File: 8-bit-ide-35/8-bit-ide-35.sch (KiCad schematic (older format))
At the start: 33 parts, among them J1 XTA_Connector, J2 IBM_8bit_DBA, J3 XTA Power, J4 LED, J5 Debug, SW1 Config, SW2 Init Drive, SW3 Reset, U1 74LVC245, U2 74LVC245, U3 74HCT125, U4 RPI_PICO, U5 74HC165

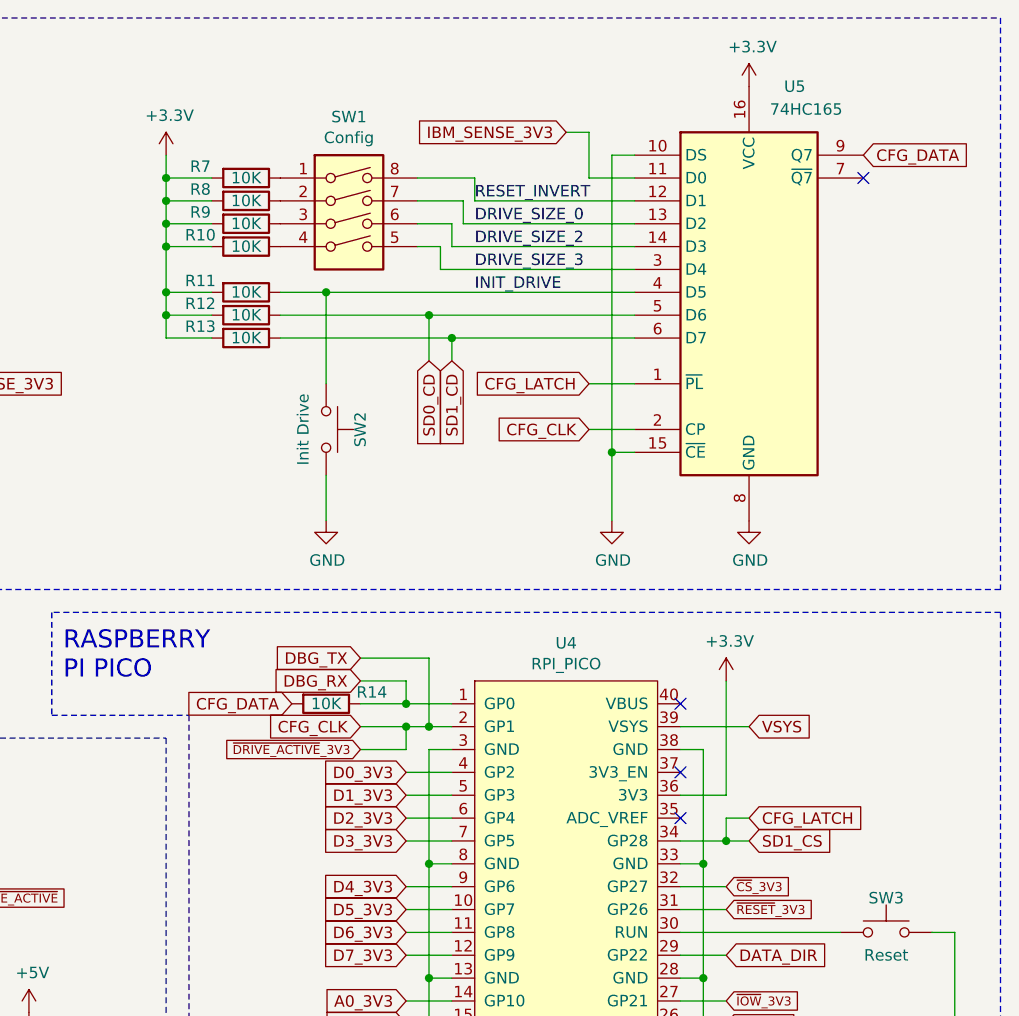
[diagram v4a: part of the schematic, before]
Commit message: Small schematic changes. Add outline of XTA board.
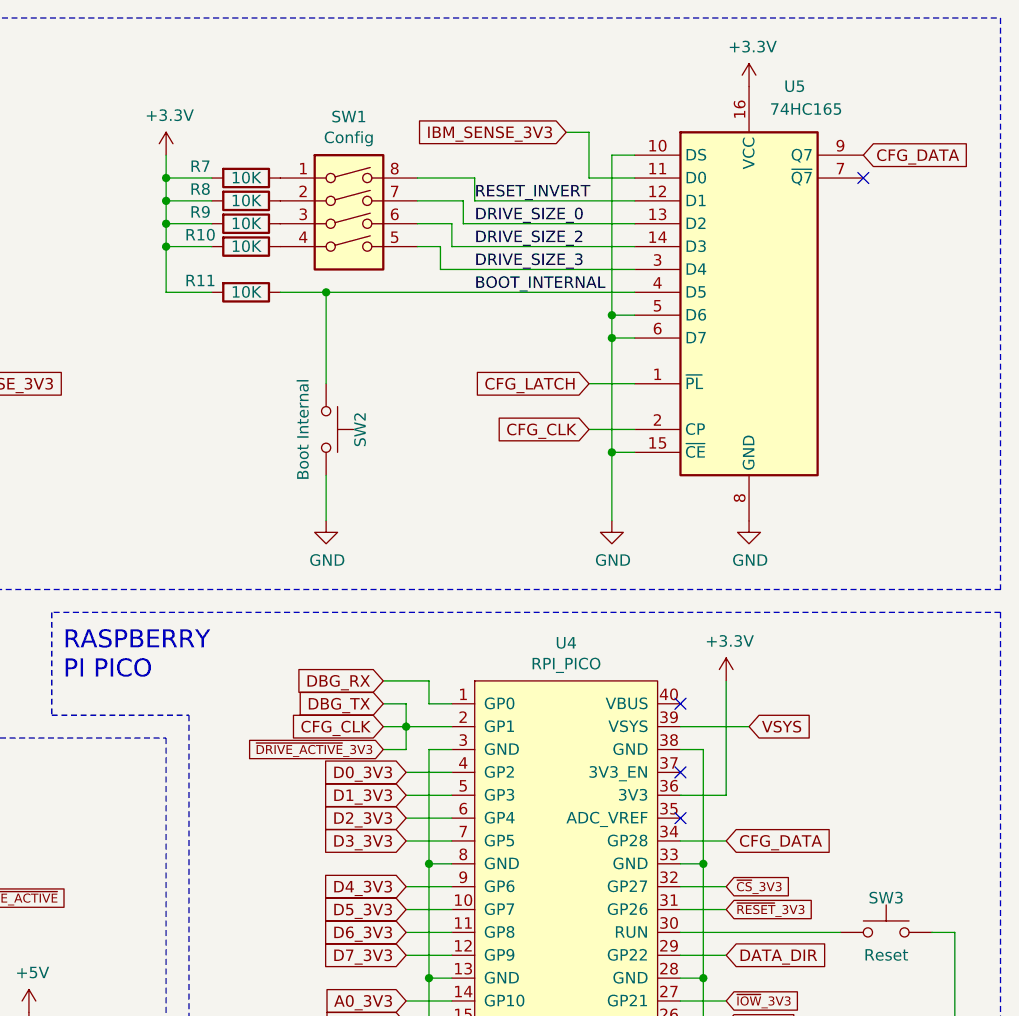
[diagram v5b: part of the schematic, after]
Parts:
- removed R12, R13, R14: 10K, Resistor_SMD:R_1206_3216Metric, symbol Device:R
- SW2: value Init Drive -> Boot Internal
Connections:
- net SD0_CD is gone; now on net GND: U5.5 (D6)
- net SD1_CD is gone; now on net GND: U5.6 (D7)
- net CFG_DATA: now also U4.34 (GP28)
- net CFG_LATCH: no longer U4.34 (GP28)
- net INIT_DRIVE renamed BOOT_INTERNAL
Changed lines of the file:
@@
 Wire Wire Line
 	9900 5050 9700 5050
-Text GLabel 8300 3750 0    39   Input ~ 0
-~DRIVE_ACTIVE~_3V3
 Text GLabel 6150 4750 0    39   Input ~ 0
 ~DRIVE_ACTIVE~_3V3
@@
 Text GLabel 9900 5150 2    50   Input ~ 0
 SD_SCK
-Text GLabel 10000 4150 2    50   Input ~ 0
-SD1_CS
-Text GLabel 8700 2050 3    50   Input ~ 0
-SD1_CD
 $Comp
 L Connector_Generic:Conn_01x06 J5
@@
 Wire Wire Line
 	9400 2450 9400 2750
-Text GLabel 8300 3650 0    50   Input ~ 0
-CFG_CLK
 Text GLabel 9300 2350 0    50   Input ~ 0
 CFG_CLK
@@
 Wire Wire Line
 	6250 2150 6350 2150
-Wire Wire Line
-	9700 4150 9900 4150
 Wire Wire Line
 	9500 1150 9400 1150
@@
 DRIVE_SIZE_3
 $Comp
-L Switch:SW_Push SW2
-U 1 1 619AC049
-P 8150 2350
-F 0 "SW2" H 8150 2500 50  0000 C CNN
-F 1 "Init Drive" H 8150 2250 50  0000 C CNN
-F 2 "" H 8150 2550 50  0001 C CNN
-F 3 "~" H 8150 2550 50  0001 C CNN
-	1    8150 2350
-	0    1    1    0
-$EndComp
-$Comp
 L power:GND #PWR027
 U 1 1 619B6D52
@@
 	8150 2550 8150 2750
 Text Label 8800 1750 0    50   ~ 0
-INIT_DRIVE
+BOOT_INTERNAL
 $Comp
 L Switch:SW_DIP_x04 SW1
@@
 	8150 1750 9500 1750
 Wire Wire Line
-	9400 1150 9400 2450
+	9400 1150 9400 1850
 Wire Wire Line
 	8550 1250 8800 1250
@@
 Wire Wire Line
 	8150 1750 8150 2150
-$Comp
-L Device:R R12
-U 1 1 61B1CB57
-P 7800 1850
-F 0 "R12" V 7750 1650 50  0000 C CNN
-F 1 "10K" V 7800 1850 50  0000 C CNN
-F 2 "Resistor_SMD:R_1206_3216Metric" V 7730 1850 50  0001 C CNN
-F 3 "~" H 7800 1850 50  0001 C CNN
-F 4 "C17902" V 7800 1850 50  0001 C CNN "LCSC"
-	1    7800 1850
-	0    1    1    0
-$EndComp
-Wire Wire Line
-	7650 1850 7450 1850
-$Comp
-L Device:R R13
-U 1 1 61B27406
-P 7800 1950
-F 0 "R13" V 7750 1750 50  0000 C CNN
-F 1 "10K" V 7800 1950 50  0000 C CNN
-F 2 "Resistor_SMD:R_1206_3216Metric" V 7730 1950 50  0001 C CNN
-F 3 "~" H 7800 1950 50  0001 C CNN
-F 4 "C17902" V 7800 1950 50  0001 C CNN "LCSC"
-	1    7800 1950
-	0    1    1    0
-$EndComp
-Wire Wire Line
-	7650 1950 7450 1950
-Wire Wire Line
-	7450 1750 7450 1850
-Connection ~ 7450 1750
-Connection ~ 7450 1850
-Wire Wire Line
-	7450 1850 7450 1950
-Wire Wire Line
-	9500 1950 8700 1950
-Wire Wire Line
-	8700 2050 8700 1950
-Connection ~ 8700 1950
-Wire Wire Line
-	8700 1950 7950 1950
 $Comp
 L Device:C C1
@@
 ~DRQ~_3V3
 Wire Wire Line
-	8300 3650 8500 3650
-Wire Wire Line
-	8300 3750 8500 3750
-Wire Wire Line
 	8500 3750 8500 3650
 Connection ~ 8500 3650
@@
 Wire Notes Line
 	7550 3600 7550 6450
-Text GLabel 10000 4050 2    50   Input ~ 0
-CFG_LATCH
-Wire Wire Line
-	10000 4050 9900 4050
-Wire Wire Line
-	9900 4050 9900 4150
-Connection ~ 9900 4150
-Wire Wire Line
-	9900 4150 10000 4150
 Text GLabel 9300 2150 0    50   Input ~ 0
 CFG_LATCH
@@
 Wire Wire Line
 	1300 7250 1550 7250
-Wire Wire Line
-	8600 1850 9500 1850
-Connection ~ 8600 1850
-Wire Wire Line
-	7950 1850 8600 1850
-Wire Wire Line
-	8600 2050 8600 1850
-Text GLabel 8600 2050 3    50   Input ~ 0
-SD0_CD
-Text GLabel 8300 3450 0    50   Input ~ 0
-DBG_RX
 Wire Wire Line
 	9900 5350 9700 5350
 Text GLabel 9900 5350 2    50   Input ~ 0
 SD0_CS
-Wire Wire Line
-	8500 3550 8500 3450
-Wire Wire Line
-	8500 3450 8300 3450
-Wire Wire Line
-	8500 3650 8600 3650
-Wire Wire Line
-	8600 3650 8700 3650
-Connection ~ 8600 3650
-Wire Wire Line
-	8600 3350 8600 3650
-Wire Wire Line
-	8500 3550 8700 3550
-Text GLabel 8300 3350 0    50   Input ~ 0
-DBG_TX
-Wire Wire Line
-	8300 3350 8600 3350
-Connection ~ 8500 3550
-Wire Wire Line
-	8300 3550 8500 3550
-Text GLabel 8000 3550 0    50   Input ~ 0
-CFG_DATA
-$Comp
-L Device:R R14
-U 1 1 6220D4A7
-P 8150 3550
-F 0 "R14" V 8100 3750 50  0000 C CNN
-F 1 "10K" V 8150 3550 50  0000 C CNN
-F 2 "Resistor_SMD:R_1206_3216Metric" V 8080 3550 50  0001 C CNN
-F 3 "~" H 8150 3550 50  0001 C CNN
-F 4 "C17902" V 8150 3550 50  0001 C CNN "LCSC"
-	1    8150 3550
-	0    1    1    0
-$EndComp
 Text Notes 7000 6700 0    39   ~ 0
 The PICO already has a 47uF cap on both the 5v and 3.3v\nside of the regulator, so none is included in this design.
+Text GLabel 9900 4150 2    50   Input ~ 0
+CFG_DATA
+Text GLabel 8400 3450 0    50   Input ~ 0
+DBG_RX
+Text GLabel 8400 3550 0    50   Input ~ 0
+DBG_TX
+Wire Wire Line
+	8400 3650 8500 3650
+Text GLabel 8400 3750 0    39   Input ~ 0
+~DRIVE_ACTIVE~_3V3
+Wire Wire Line
+	8400 3750 8500 3750
+Text GLabel 8400 3650 0    50   Input ~ 0
+CFG_CLK
+Wire Wire Line
+	8500 3650 8700 3650
+Wire Wire Line
+	9900 4150 9700 4150
+Wire Wire Line
+	8400 3550 8500 3550
+Wire Wire Line
+	8500 3550 8500 3650
+Wire Wire Line
+	8400 3450 8600 3450
+Wire Wire Line
+	8600 3450 8600 3550
+Wire Wire Line
+	8600 3550 8700 3550
+$Comp
+L Switch:SW_Push SW2
+U 1 1 619AC049
+P 8150 2350
+F 0 "SW2" H 8150 2500 50  0000 C CNN
+F 1 "Boot Internal" H 8150 2250 50  0000 C CNN
+F 2 "" H 8150 2550 50  0001 C CNN
+F 3 "~" H 8150 2550 50  0001 C CNN
+	1    8150 2350
+	0    1    1    0
+$EndComp
+Wire Wire Line
+	9500 1850 9400 1850
+Connection ~ 9400 1850
+Wire Wire Line
+	9400 1850 9400 1950
+Wire Wire Line
+	9500 1950 9400 1950
+Connection ~ 9400 1950
+Wire Wire Line
+	9400 1950 9400 2450
 $EndSCHEMATC
